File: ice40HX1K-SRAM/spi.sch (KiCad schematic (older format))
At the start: 9 parts

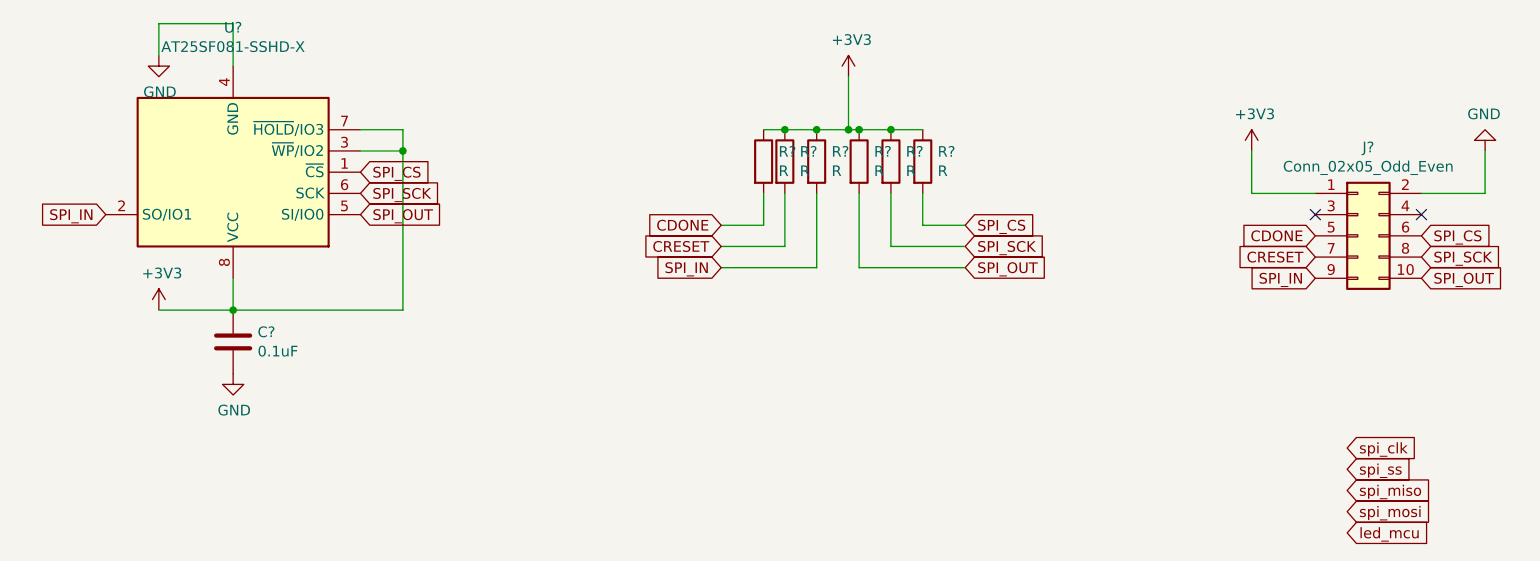
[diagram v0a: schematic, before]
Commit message: wiring FPGA nRF52 and ATSAMD11
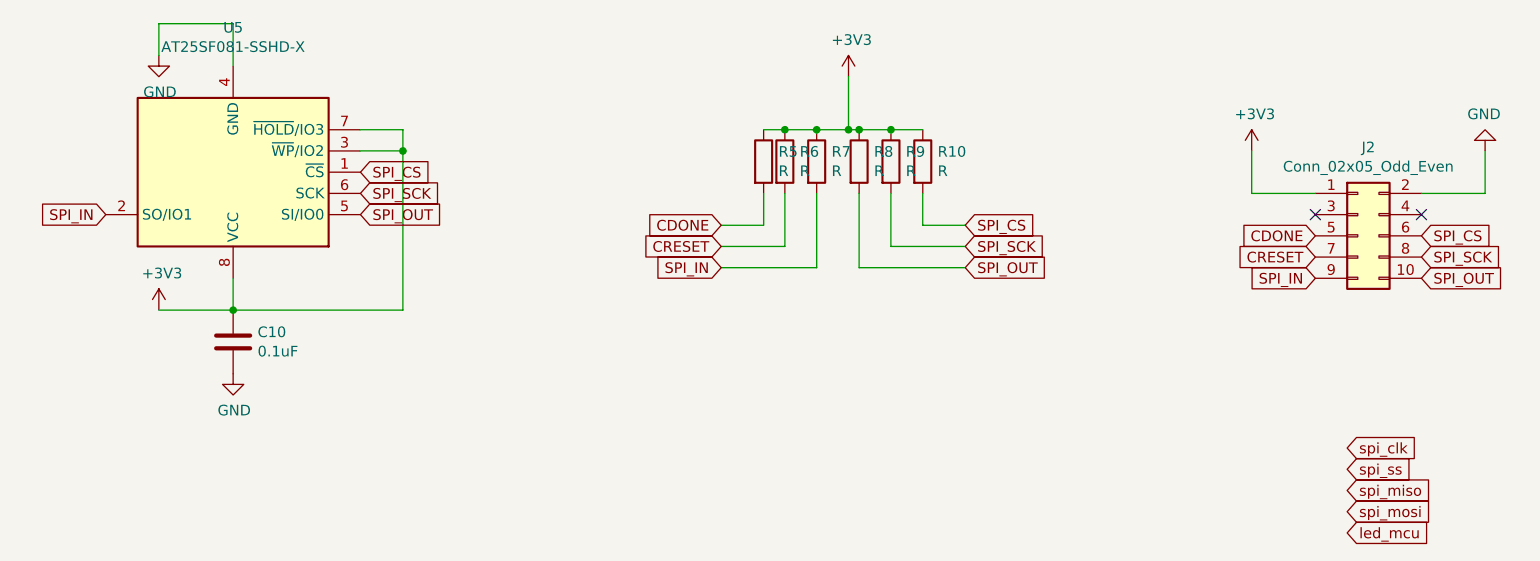
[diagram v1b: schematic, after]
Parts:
- gave numbers to parts that had none: 9
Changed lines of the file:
@@
 P 2300 1900
 AR Path="/5E610BE8" Ref="U?"  Part="1"
-AR Path="/5E5F2441/5E610BE8" Ref="U?"  Part="1"
-F 0 "U?" H 2300 1219 50  0000 C CNN
+AR Path="/5E5F2441/5E610BE8" Ref="U5"  Part="1"
+F 0 "U5" H 2300 1219 50  0000 C CNN
 F 1 "AT25SF081-SSHD-X" H 2300 1310 50  0000 C CNN
 F 2 "Package_SO:SOIC-8_3.9x4.9mm_P1.27mm" H 2300 1300 50  0001 C CNN
@@
 P 2300 2700
 AR Path="/5E610BEE" Ref="C?"  Part="1"
-AR Path="/5E5F2441/5E610BEE" Ref="C?"  Part="1"
-F 0 "C?" H 2415 2746 50  0000 L CNN
+AR Path="/5E5F2441/5E610BEE" Ref="C10"  Part="1"
+F 0 "C10" H 2415 2746 50  0000 L CNN
 F 1 "0.1uF" H 2415 2655 50  0000 L CNN
 F 2 "Capacitor_SMD:C_0805_2012Metric" H 2338 2550 50  0001 C CNN
@@
 P 1950 2550
 AR Path="/5E610BF4" Ref="#PWR?"  Part="1"
-AR Path="/5E5F2441/5E610BF4" Ref="#PWR?"  Part="1"
-F 0 "#PWR?" H 1950 2400 50  0001 C CNN
+AR Path="/5E5F2441/5E610BF4" Ref="#PWR013"  Part="1"
+F 0 "#PWR013" H 1950 2400 50  0001 C CNN
 F 1 "+3V3" H 1965 2723 50  0000 C CNN
 F 2 "" H 1950 2550 50  0001 C CNN
@@
 P 2300 2850
 AR Path="/5E610C07" Ref="#PWR?"  Part="1"
-AR Path="/5E5F2441/5E610C07" Ref="#PWR?"  Part="1"
-F 0 "#PWR?" H 2300 2600 50  0001 C CNN
+AR Path="/5E5F2441/5E610C07" Ref="#PWR014"  Part="1"
+F 0 "#PWR014" H 2300 2600 50  0001 C CNN
 F 1 "GND" H 2305 2677 50  0000 C CNN
 F 2 "" H 2300 2850 50  0001 C CNN
@@
 P 1950 1350
 AR Path="/5E610C0D" Ref="#PWR?"  Part="1"
-AR Path="/5E5F2441/5E610C0D" Ref="#PWR?"  Part="1"
-F 0 "#PWR?" H 1950 1100 50  0001 C CNN
+AR Path="/5E5F2441/5E610C0D" Ref="#PWR012"  Part="1"
+F 0 "#PWR012" H 1950 1100 50  0001 C CNN
 F 1 "GND" H 1955 1177 50  0000 C CNN
 F 2 "" H 1950 1350 50  0001 C CNN
@@
 P 5050 1850
 AR Path="/5E62B581" Ref="R?"  Part="1"
-AR Path="/5E5F2441/5E62B581" Ref="R?"  Part="1"
-F 0 "R?" H 5120 1896 50  0000 L CNN
+AR Path="/5E5F2441/5E62B581" Ref="R7"  Part="1"
+F 0 "R7" H 5120 1896 50  0000 L CNN
 F 1 "R" H 5120 1805 50  0000 L CNN
 F 2 "Resistor_SMD:R_1206_3216Metric" V 4980 1850 50  0001 C CNN
@@
 P 5250 1850
 AR Path="/5E62B587" Ref="R?"  Part="1"
-AR Path="/5E5F2441/5E62B587" Ref="R?"  Part="1"
-F 0 "R?" H 5320 1896 50  0000 L CNN
+AR Path="/5E5F2441/5E62B587" Ref="R8"  Part="1"
+F 0 "R8" H 5320 1896 50  0000 L CNN
 F 1 "R" H 5320 1805 50  0000 L CNN
 F 2 "Resistor_SMD:R_1206_3216Metric" V 5180 1850 50  0001 C CNN
@@
 P 5400 1850
 AR Path="/5E62B58D" Ref="R?"  Part="1"
-AR Path="/5E5F2441/5E62B58D" Ref="R?"  Part="1"
-F 0 "R?" H 5470 1896 50  0000 L CNN
+AR Path="/5E5F2441/5E62B58D" Ref="R9"  Part="1"
+F 0 "R9" H 5470 1896 50  0000 L CNN
 F 1 "R" H 5470 1805 50  0000 L CNN
 F 2 "Resistor_SMD:R_1206_3216Metric" V 5330 1850 50  0001 C CNN
@@
 P 5550 1850
 AR Path="/5E62B593" Ref="R?"  Part="1"
-AR Path="/5E5F2441/5E62B593" Ref="R?"  Part="1"
-F 0 "R?" H 5620 1896 50  0000 L CNN
+AR Path="/5E5F2441/5E62B593" Ref="R10"  Part="1"
+F 0 "R10" H 5620 1896 50  0000 L CNN
 F 1 "R" H 5620 1805 50  0000 L CNN
 F 2 "Resistor_SMD:R_1206_3216Metric" V 5480 1850 50  0001 C CNN
@@
 P 4800 1850
 AR Path="/5E62B599" Ref="R?"  Part="1"
-AR Path="/5E5F2441/5E62B599" Ref="R?"  Part="1"
-F 0 "R?" H 4870 1896 50  0000 L CNN
+AR Path="/5E5F2441/5E62B599" Ref="R5"  Part="1"
+F 0 "R5" H 4870 1896 50  0000 L CNN
 F 1 "R" H 4870 1805 50  0000 L CNN
 F 2 "Resistor_SMD:R_1206_3216Metric" V 4730 1850 50  0001 C CNN
@@
 P 4900 1850
 AR Path="/5E62B59F" Ref="R?"  Part="1"
-AR Path="/5E5F2441/5E62B59F" Ref="R?"  Part="1"
-F 0 "R?" H 4970 1896 50  0000 L CNN
+AR Path="/5E5F2441/5E62B59F" Ref="R6"  Part="1"
+F 0 "R6" H 4970 1896 50  0000 L CNN
 F 1 "R" H 4970 1805 50  0000 L CNN
 F 2 "Resistor_SMD:R_1206_3216Metric" V 4830 1850 50  0001 C CNN
@@
 P 5200 1450
 AR Path="/5E62B5AB" Ref="#PWR?"  Part="1"
-AR Path="/5E5F2441/5E62B5AB" Ref="#PWR?"  Part="1"
-F 0 "#PWR?" H 5200 1300 50  0001 C CNN
+AR Path="/5E5F2441/5E62B5AB" Ref="#PWR015"  Part="1"
+F 0 "#PWR015" H 5200 1300 50  0001 C CNN
 F 1 "+3V3" H 5215 1623 50  0000 C CNN
 F 2 "" H 5200 1450 50  0001 C CNN
@@
 	5550 2150 5750 2150
 $Comp
-L Connector_Generic:Conn_02x05_Odd_Even J?
+L Connector_Generic:Conn_02x05_Odd_Even J2
 U 1 1 5E63A010
 P 7600 2200
-F 0 "J?" H 7650 2617 50  0000 C CNN
+F 0 "J2" H 7650 2617 50  0000 C CNN
 F 1 "Conn_02x05_Odd_Even" H 7650 2526 50  0000 C CNN
 F 2 "Connector_PinHeader_2.54mm:PinHeader_2x05_P2.54mm_Vertical" H 7600 2200 50  0001 C CNN
@@
 CRESET
 $Comp
-L power:+3V3 #PWR?
+L power:+3V3 #PWR016
 U 1 1 5E63A01C
 P 7100 1800
-F 0 "#PWR?" H 7100 1650 50  0001 C CNN
+F 0 "#PWR016" H 7100 1650 50  0001 C CNN
 F 1 "+3V3" H 7115 1973 50  0000 C CNN
 F 2 "" H 7100 1800 50  0001 C CNN
@@
 $EndComp
 $Comp
-L power:GND #PWR?
+L power:GND #PWR017
 U 1 1 5E63A022
 P 8200 1800
-F 0 "#PWR?" H 8200 1550 50  0001 C CNN
+F 0 "#PWR017" H 8200 1550 50  0001 C CNN
 F 1 "GND" H 8205 1627 50  0000 C CNN
 F 2 "" H 8200 1800 50  0001 C CNN

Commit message: wiring FPGA
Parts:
- C10: footprint Capacitor_SMD:C_0805_2012Metric -> Capacitor_SMD:C_0402_1005Metric
- R10, R5, R6, R7, R8, R9: value R -> 10kOhm; footprint Resistor_SMD:R_1206_3216Metric -> Resistor_SMD:R_0402_1005Metric
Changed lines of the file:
@@
 F 0 "C10" H 2415 2746 50  0000 L CNN
 F 1 "0.1uF" H 2415 2655 50  0000 L CNN
-F 2 "Capacitor_SMD:C_0805_2012Metric" H 2338 2550 50  0001 C CNN
+F 2 "Capacitor_SMD:C_0402_1005Metric" H 2338 2550 50  0001 C CNN
 F 3 "~" H 2300 2700 50  0001 C CNN
 	1    2300 2700
@@
 AR Path="/5E5F2441/5E62B581" Ref="R7"  Part="1"
 F 0 "R7" H 5120 1896 50  0000 L CNN
-F 1 "R" H 5120 1805 50  0000 L CNN
-F 2 "Resistor_SMD:R_1206_3216Metric" V 4980 1850 50  0001 C CNN
+F 1 "10kOhm" H 5120 1805 50  0000 L CNN
+F 2 "Resistor_SMD:R_0402_1005Metric" V 4980 1850 50  0001 C CNN
 F 3 "~" H 5050 1850 50  0001 C CNN
 	1    5050 1850
@@
 AR Path="/5E5F2441/5E62B587" Ref="R8"  Part="1"
 F 0 "R8" H 5320 1896 50  0000 L CNN
-F 1 "R" H 5320 1805 50  0000 L CNN
-F 2 "Resistor_SMD:R_1206_3216Metric" V 5180 1850 50  0001 C CNN
+F 1 "10kOhm" H 5320 1805 50  0000 L CNN
+F 2 "Resistor_SMD:R_0402_1005Metric" V 5180 1850 50  0001 C CNN
 F 3 "~" H 5250 1850 50  0001 C CNN
 	1    5250 1850
@@
 AR Path="/5E5F2441/5E62B58D" Ref="R9"  Part="1"
 F 0 "R9" H 5470 1896 50  0000 L CNN
-F 1 "R" H 5470 1805 50  0000 L CNN
-F 2 "Resistor_SMD:R_1206_3216Metric" V 5330 1850 50  0001 C CNN
+F 1 "10kOhm" H 5470 1805 50  0000 L CNN
+F 2 "Resistor_SMD:R_0402_1005Metric" V 5330 1850 50  0001 C CNN
 F 3 "~" H 5400 1850 50  0001 C CNN
 	1    5400 1850
@@
 AR Path="/5E5F2441/5E62B593" Ref="R10"  Part="1"
 F 0 "R10" H 5620 1896 50  0000 L CNN
-F 1 "R" H 5620 1805 50  0000 L CNN
-F 2 "Resistor_SMD:R_1206_3216Metric" V 5480 1850 50  0001 C CNN
+F 1 "10kOhm" H 5620 1805 50  0000 L CNN
+F 2 "Resistor_SMD:R_0402_1005Metric" V 5480 1850 50  0001 C CNN
 F 3 "~" H 5550 1850 50  0001 C CNN
 	1    5550 1850
@@
 AR Path="/5E5F2441/5E62B599" Ref="R5"  Part="1"
 F 0 "R5" H 4870 1896 50  0000 L CNN
-F 1 "R" H 4870 1805 50  0000 L CNN
-F 2 "Resistor_SMD:R_1206_3216Metric" V 4730 1850 50  0001 C CNN
+F 1 "10kOhm" H 4870 1805 50  0000 L CNN
+F 2 "Resistor_SMD:R_0402_1005Metric" V 4730 1850 50  0001 C CNN
 F 3 "~" H 4800 1850 50  0001 C CNN
 	1    4800 1850
@@
 AR Path="/5E5F2441/5E62B59F" Ref="R6"  Part="1"
 F 0 "R6" H 4970 1896 50  0000 L CNN
-F 1 "R" H 4970 1805 50  0000 L CNN
-F 2 "Resistor_SMD:R_1206_3216Metric" V 4830 1850 50  0001 C CNN
+F 1 "10kOhm" H 4970 1805 50  0000 L CNN
+F 2 "Resistor_SMD:R_0402_1005Metric" V 4830 1850 50  0001 C CNN
 F 3 "~" H 4900 1850 50  0001 C CNN
 	1    4900 1850
@@
 NoConn ~ 7900 2100
 NoConn ~ 7400 2100
-Text GLabel 7550 3200 2    50   Input ~ 0
-spi_clk
-Text GLabel 7550 3300 2    50   Input ~ 0
-spi_ss
-Text GLabel 7550 3400 2    50   Input ~ 0
-spi_miso
-Text GLabel 7550 3500 2    50   Input ~ 0
-spi_mosi
-Text GLabel 7550 3600 2    50   Input ~ 0
-led_mcu
 $EndSCHEMATC
